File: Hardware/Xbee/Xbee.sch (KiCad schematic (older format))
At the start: 44 parts, among them J1 Alimentación, J2 Raspberry, J3 Pines 1, J4 Pines 2, J5 Programación, J6 Entrada, J7 Salida, K1 Rele12V, Q1 BC338, Q2 BC338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

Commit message: Started routing
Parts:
- D5, D6: footprint LED_THT:LED_D5.0mm -> Connector_PinSocket_2.54mm:PinSocket_1x02_P2.54mm_Vertical
- renumbered R4 to R1, R1 to R2, R2 to R3, R3 to R4
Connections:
- net GNDREF: now also J6.1 (Pin_1); no longer J6.2 (Pin_2)
- net Rasp.In: now also J6.2 (Pin_2); no longer J6.1 (Pin_1)

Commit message: Routing
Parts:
- C2: value 10u -> 1u
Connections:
- net Rasp.In renamed DIO2-Entrada
- net Rasp.Out renamed DIO2-Salida
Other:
- moved on the sheet: D4, D7, J6, J7, JP3, JP4, K1, Q2, Q3, R10, R13, R5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

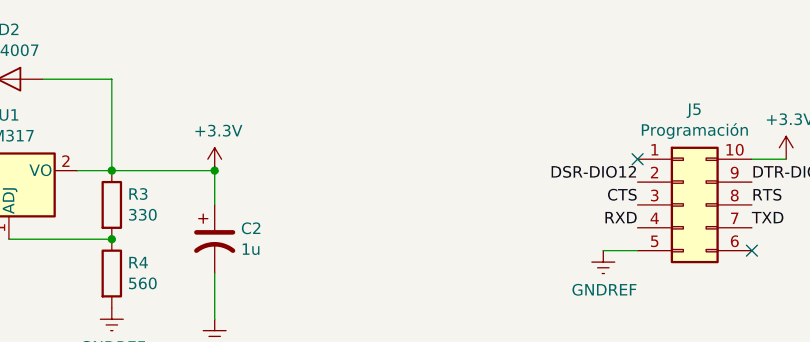
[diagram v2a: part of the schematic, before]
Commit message: SMD footprint
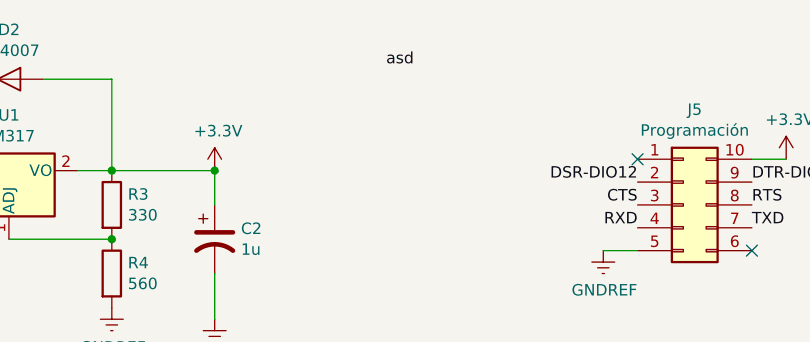
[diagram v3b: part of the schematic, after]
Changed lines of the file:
@@
 Text Label 8550 5350 0    50   ~ 0
 DIO2-Salida
+Text Label 4450 850  0    50   ~ 0
+asd
 $EndSCHEMATC

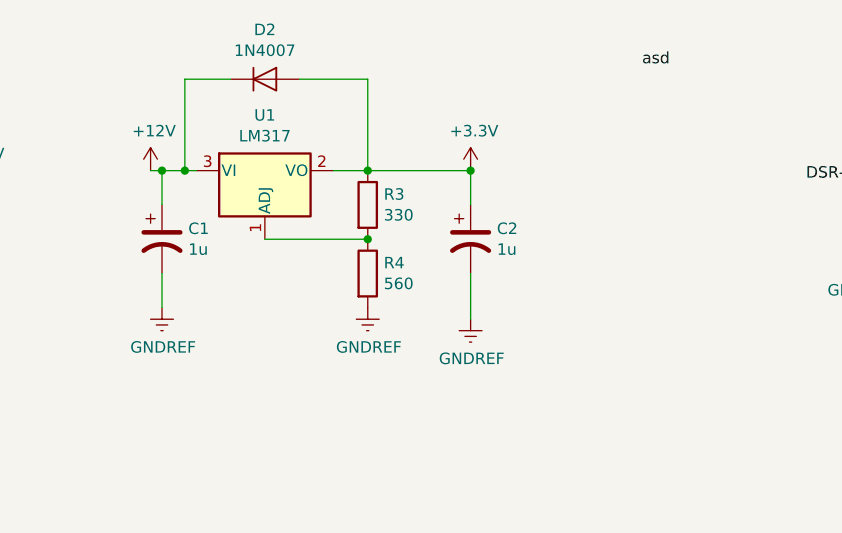
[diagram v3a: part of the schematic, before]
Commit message: SMD components
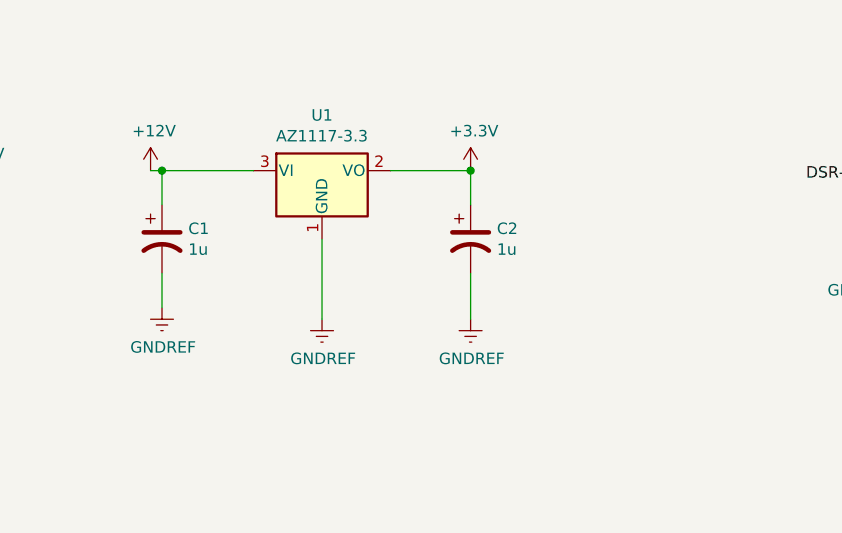
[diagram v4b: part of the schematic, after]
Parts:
- removed D2: 1N4007, Diode_THT:D_DO-41_SOD81_P10.16mm_Horizontal, symbol Xbee-rescue:1N4007-Diode
- removed R3: 330, Resistor_THT:R_Axial_DIN0207_L6.3mm_D2.5mm_P10.16mm_Horizontal, symbol Xbee-rescue:R-Device
- removed R4: 560, Resistor_THT:R_Axial_DIN0207_L6.3mm_D2.5mm_P10.16mm_Horizontal, symbol Xbee-rescue:R-Device
- removed U1: LM317, Package_TO_SOT_THT:TO-220-3_Vertical, symbol Xbee-rescue:LM317_3PinPackage-Regulator_Linear
- added U1: AZ1117-3.3, Package_TO_SOT_SMD:SOT-223-3_TabPin2, symbol Regulator_Linear:AZ1117-3.3
- D1, D7: footprint LED_THT:LED_D5.0mm -> LED_SMD:LED_0805_2012Metric
- U3: footprint Package_DIP:DIP-8_W7.62mm_Socket_LongPads -> Package_SO:SO-8_3.9x4.9mm_P1.27mm
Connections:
- net +12V: now also U1.3 (VI)
- net +3V3: now also U1.2 (VO)
- net GNDREF: now also U1.1 (GND)
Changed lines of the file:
@@
 	1550 1400 1400 1400
-$Comp
-L Xbee-rescue:LM317_3PinPackage-Regulator_Linear U1
-U 1 1 5C054755
-P 2800 1300
-F 0 "U1" H 2800 1542 50  0000 C CNN
-F 1 "LM317" H 2800 1451 50  0000 C CNN
-F 2 "Package_TO_SOT_THT:TO-220-3_Vertical" H 2800 1550 50  0001 C CIN
-F 3 "http://www.ti.com/lit/ds/symlink/lm317.pdf" H 2800 1300 50  0001 C CNN
-	1    2800 1300
-	1    0    0    -1
-$EndComp
-$Comp
-L Xbee-rescue:R-Device R3
-U 1 1 5C054800
-P 3250 1450
-F 0 "R3" H 3320 1496 50  0000 L CNN
-F 1 "330" H 3320 1405 50  0000 L CNN
-F 2 "Resistor_THT:R_Axial_DIN0207_L6.3mm_D2.5mm_P10.16mm_Horizontal" V 3180 1450 50  0001 C CNN
-F 3 "~" H 3250 1450 50  0001 C CNN
-	1    3250 1450
-	1    0    0    -1
-$EndComp
-$Comp
-L Xbee-rescue:R-Device R4
-U 1 1 5C054888
-P 3250 1750
-F 0 "R4" H 3320 1796 50  0000 L CNN
-F 1 "560" H 3320 1705 50  0000 L CNN
-F 2 "Resistor_THT:R_Axial_DIN0207_L6.3mm_D2.5mm_P10.16mm_Horizontal" V 3180 1750 50  0001 C CNN
-F 3 "~" H 3250 1750 50  0001 C CNN
-	1    3250 1750
-	1    0    0    -1
-$EndComp
 $Comp
 L Xbee-rescue:GNDREF-power #PWR012
 U 1 1 5C0548D0
-P 3250 1900
-F 0 "#PWR012" H 3250 1650 50  0001 C CNN
-F 1 "GNDREF" H 3255 1727 50  0000 C CNN
-F 2 "" H 3250 1900 50  0001 C CNN
-F 3 "" H 3250 1900 50  0001 C CNN
-	1    3250 1900
-	1    0    0    -1
-$EndComp
-Wire Wire Line
-	3250 1600 2800 1600
-Connection ~ 3250 1600
-Wire Wire Line
-	3100 1300 3250 1300
+P 3050 1950
+F 0 "#PWR012" H 3050 1700 50  0001 C CNN
+F 1 "GNDREF" H 3055 1777 50  0000 C CNN
+F 2 "" H 3050 1950 50  0001 C CNN
+F 3 "" H 3050 1950 50  0001 C CNN
+	1    3050 1950
+	1    0    0    -1
+$EndComp
 $Comp
 L Xbee-rescue:+12V-power #PWR07
@@
 Connection ~ 2350 1300
 Wire Wire Line
-	2350 1300 2450 1300
-Wire Wire Line
 	3700 1450 3700 1300
-Wire Wire Line
-	3700 1300 3250 1300
-Connection ~ 3250 1300
-$Comp
-L Xbee-rescue:1N4007-Diode D2
-U 1 1 5C054DA4
-P 2800 900
-F 0 "D2" H 2800 1116 50  0000 C CNN
-F 1 "1N4007" H 2800 1025 50  0000 C CNN
-F 2 "Diode_THT:D_DO-41_SOD81_P10.16mm_Horizontal" H 2800 725 50  0001 C CNN
-F 3 "http://www.vishay.com/docs/88503/1n4001.pdf" H 2800 900 50  0001 C CNN
-	1    2800 900
-	1    0    0    -1
-$EndComp
-Wire Wire Line
-	2650 900  2450 900
-Wire Wire Line
-	2450 900  2450 1300
-Connection ~ 2450 1300
-Wire Wire Line
-	2450 1300 2500 1300
-Wire Wire Line
-	2950 900  3250 900
-Wire Wire Line
-	3250 900  3250 1300
 $Comp
 L Xbee-rescue:SW_Push_Dual-Switch SW1
@@
 	1    0    0    -1
 $EndComp
-Connection ~ 3700 1300
 NoConn ~ 6750 3300
 Text Label 4550 3100 2    50   ~ 0
@@
 F 0 "D1" V 1738 6032 50  0000 R CNN
 F 1 "Assoc-RSSI" V 1647 6032 50  0000 R CNN
-F 2 "LED_THT:LED_D5.0mm" H 1700 6150 50  0001 C CNN
+F 2 "LED_SMD:LED_0805_2012Metric" H 1700 6150 50  0001 C CNN
 F 3 "~" H 1700 6150 50  0001 C CNN
 	1    1700 6150
@@
 F 0 "U3" H 9250 1567 50  0000 C CNN
 F 1 "LM358" H 9250 1476 50  0000 C CNN
-F 2 "Package_DIP:DIP-8_W7.62mm_Socket_LongPads" H 9250 1200 50  0001 C CNN
+F 2 "Package_SO:SO-8_3.9x4.9mm_P1.27mm" H 9250 1200 50  0001 C CNN
 F 3 "http://www.ti.com/lit/ds/symlink/lm2904-n.pdf" H 9250 1200 50  0001 C CNN
 	1    9250 1200
@@
 F 0 "U3" H 9250 2367 50  0000 C CNN
 F 1 "LM358" H 9250 2276 50  0000 C CNN
-F 2 "Package_DIP:DIP-8_W7.62mm_Socket_LongPads" H 9250 2000 50  0001 C CNN
+F 2 "Package_SO:SO-8_3.9x4.9mm_P1.27mm" H 9250 2000 50  0001 C CNN
 F 3 "http://www.ti.com/lit/ds/symlink/lm2904-n.pdf" H 9250 2000 50  0001 C CNN
 	2    9250 2000
@@
 F 0 "U3" H 7608 1396 50  0000 L CNN
 F 1 "LM358" H 7608 1305 50  0000 L CNN
-F 2 "Package_DIP:DIP-8_W7.62mm_Socket_LongPads" H 7650 1350 50  0001 C CNN
+F 2 "Package_SO:SO-8_3.9x4.9mm_P1.27mm" H 7650 1350 50  0001 C CNN
 F 3 "http://www.ti.com/lit/ds/symlink/lm2904-n.pdf" H 7650 1350 50  0001 C CNN
 	3    7650 1350
@@
 F 0 "D7" V 10638 5982 50  0000 R CNN
 F 1 "LED Salida" V 10547 5982 50  0000 R CNN
-F 2 "LED_THT:LED_D5.0mm" H 10600 6100 50  0001 C CNN
+F 2 "LED_SMD:LED_0805_2012Metric" H 10600 6100 50  0001 C CNN
 F 3 "~" H 10600 6100 50  0001 C CNN
 	1    10600 6100
@@
 Text Label 8550 5350 0    50   ~ 0
 DIO2-Salida
-Text Label 4450 850  0    50   ~ 0
-asd
+$Comp
+L Regulator_Linear:AZ1117-3.3 U1
+U 1 1 5D4F039F
+P 3050 1300
+F 0 "U1" H 3050 1542 50  0000 C CNN
+F 1 "AZ1117-3.3" H 3050 1451 50  0000 C CNN
+F 2 "Package_TO_SOT_SMD:SOT-223-3_TabPin2" H 3050 1550 50  0001 C CIN
+F 3 "https://www.diodes.com/assets/Datasheets/AZ1117.pdf" H 3050 1300 50  0001 C CNN
+	1    3050 1300
+	1    0    0    -1
+$EndComp
+Wire Wire Line
+	2350 1300 2750 1300
+Wire Wire Line
+	3350 1300 3700 1300
+Connection ~ 3700 1300
+Wire Wire Line
+	3050 1600 3050 1950
 $EndSCHEMATC

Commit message: Change names
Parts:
- D1: value Assoc-RSSI -> Blue Assoc-RSSI
- D7: value LED Salida -> LED Green Salida
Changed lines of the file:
@@
 P 1700 6150
 F 0 "D1" V 1738 6032 50  0000 R CNN
-F 1 "Assoc-RSSI" V 1647 6032 50  0000 R CNN
+F 1 "Blue Assoc-RSSI" V 1647 6032 50  0000 R CNN
 F 2 "LED_SMD:LED_0805_2012Metric" H 1700 6150 50  0001 C CNN
 F 3 "~" H 1700 6150 50  0001 C CNN
@@
 P 10600 6100
 F 0 "D7" V 10638 5982 50  0000 R CNN
-F 1 "LED Salida" V 10547 5982 50  0000 R CNN
+F 1 "LED Green Salida" V 10547 5982 50  0000 R CNN
 F 2 "LED_SMD:LED_0805_2012Metric" H 10600 6100 50  0001 C CNN
 F 3 "~" H 10600 6100 50  0001 C CNN

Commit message: SMD footprints, change LED's
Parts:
- removed Q1: BC338, Package_TO_SOT_THT:TO-92_Inline, symbol Xbee-rescue:BC338-Transistor_BJT
- removed R2: 68, Resistor_THT:R_Axial_DIN0207_L6.3mm_D2.5mm_P10.16mm_Horizontal, symbol Xbee-rescue:R-Device
- C1, C2: footprint Capacitor_THT:CP_Radial_D5.0mm_P2.50mm -> Capacitor_SMD:C_0805_2012Metric
- D3: footprint Diode_THT:D_DO-35_SOD27_P10.16mm_Horizontal -> Diode_SMD:D_SOT-23_ANK
- J5: footprint Connector_PinHeader_2.54mm:PinHeader_2x05_P2.54mm_Vertical -> Connector_PinHeader_2.54mm:PinHeader_2x05_P2.54mm_Horizontal
- R1: value 330 -> 360
- R13: value 680 -> 4k7
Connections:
- net at D1.2 (A): now also R1.1
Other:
- moved on the sheet: D1
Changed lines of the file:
@@
 F 0 "C1" H 2465 1646 50  0000 L CNN
 F 1 "1u" H 2465 1555 50  0000 L CNN
-F 2 "Capacitor_THT:CP_Radial_D5.0mm_P2.50mm" H 2350 1600 50  0001 C CNN
+F 2 "Capacitor_SMD:C_0805_2012Metric" H 2350 1600 50  0001 C CNN
 F 3 "~" H 2350 1600 50  0001 C CNN
 	1    2350 1600
@@
 F 0 "C2" H 3815 1646 50  0000 L CNN
 F 1 "1u" H 3815 1555 50  0000 L CNN
-F 2 "Capacitor_THT:CP_Radial_D5.0mm_P2.50mm" H 3700 1600 50  0001 C CNN
+F 2 "Capacitor_SMD:C_0805_2012Metric" H 3700 1600 50  0001 C CNN
 F 3 "~" H 3700 1600 50  0001 C CNN
 	1    3700 1600
@@
 Assoc.
 $Comp
-L Xbee-rescue:R-Device R2
-U 1 1 5C1A5BA0
-P 1700 5850
-F 0 "R2" H 1770 5896 50  0000 L CNN
-F 1 "68" H 1770 5805 50  0000 L CNN
-F 2 "Resistor_THT:R_Axial_DIN0207_L6.3mm_D2.5mm_P10.16mm_Horizontal" V 1630 5850 50  0001 C CNN
-F 3 "~" H 1700 5850 50  0001 C CNN
-	1    1700 5850
-	1    0    0    -1
-$EndComp
-$Comp
 L Xbee-rescue:LED_ALT-Device D1
 U 1 1 5C1A5C83
-P 1700 6150
-F 0 "D1" V 1738 6032 50  0000 R CNN
-F 1 "Blue Assoc-RSSI" V 1647 6032 50  0000 R CNN
-F 2 "LED_SMD:LED_0805_2012Metric" H 1700 6150 50  0001 C CNN
-F 3 "~" H 1700 6150 50  0001 C CNN
-	1    1700 6150
+P 1400 5650
+F 0 "D1" V 1438 5532 50  0000 R CNN
+F 1 "Blue Assoc-RSSI" V 1347 5532 50  0000 R CNN
+F 2 "LED_SMD:LED_0805_2012Metric" H 1400 5650 50  0001 C CNN
+F 3 "~" H 1400 5650 50  0001 C CNN
+	1    1400 5650
 	0    -1   -1   0
 $EndComp
@@
 L Xbee-rescue:GNDREF-power #PWR06
 U 1 1 5C1A5D78
-P 1700 6400
-F 0 "#PWR06" H 1700 6150 50  0001 C CNN
-F 1 "GNDREF" H 1705 6227 50  0000 C CNN
-F 2 "" H 1700 6400 50  0001 C CNN
-F 3 "" H 1700 6400 50  0001 C CNN
-	1    1700 6400
+P 1400 5900
+F 0 "#PWR06" H 1400 5650 50  0001 C CNN
+F 1 "GNDREF" H 1405 5727 50  0000 C CNN
+F 2 "" H 1400 5900 50  0001 C CNN
+F 3 "" H 1400 5900 50  0001 C CNN
+	1    1400 5900
 	1    0    0    -1
 $EndComp
@@
 F 0 "J5" H 5800 1867 50  0000 C CNN
 F 1 "Programación" H 5800 1776 50  0000 C CNN
-F 2 "Connector_PinHeader_2.54mm:PinHeader_2x05_P2.54mm_Vertical" H 5750 1450 50  0001 C CNN
+F 2 "Connector_PinHeader_2.54mm:PinHeader_2x05_P2.54mm_Horizontal" H 5750 1450 50  0001 C CNN
 F 3 "~" H 5750 1450 50  0001 C CNN
 	1    5750 1450
@@
 	0    -1   -1   0
 $EndComp
-$Comp
-L Xbee-rescue:BC338-Transistor_BJT Q1
-U 1 1 5C1A9F9C
-P 1600 5500
-F 0 "Q1" H 1791 5546 50  0000 L CNN
-F 1 "BC338" H 1791 5455 50  0000 L CNN
-F 2 "Package_TO_SOT_THT:TO-92_Inline" H 1800 5425 50  0001 L CIN
-F 3 "http://diotec.com/tl_files/diotec/files/pdf/datasheets/bc337" H 1600 5500 50  0001 L CNN
-	1    1600 5500
-	1    0    0    -1
-$EndComp
 Text Label 950  5250 2    50   ~ 0
 RSSI
@@
 P 1250 5500
 F 0 "R1" V 1043 5500 50  0000 C CNN
-F 1 "330" V 1134 5500 50  0000 C CNN
+F 1 "360" V 1134 5500 50  0000 C CNN
 F 2 "Resistor_THT:R_Axial_DIN0207_L6.3mm_D2.5mm_P10.16mm_Horizontal" V 1180 5500 50  0001 C CNN
 F 3 "~" H 1250 5500 50  0001 C CNN
@@
 	0    1    1    0
 $EndComp
-$Comp
-L Xbee-rescue:+3.3V-power #PWR05
-U 1 1 5C1AB37D
-P 1700 5300
-F 0 "#PWR05" H 1700 5150 50  0001 C CNN
-F 1 "+3.3V" H 1715 5473 50  0000 C CNN
-F 2 "" H 1700 5300 50  0001 C CNN
-F 3 "" H 1700 5300 50  0001 C CNN
-	1    1700 5300
-	1    0    0    -1
-$EndComp
-Wire Wire Line
-	1700 6300 1700 6400
+Wire Wire Line
+	1400 5800 1400 5900
 $Comp
 L Xbee-rescue:Screw_Terminal_01x02-Connector J7
@@
 F 0 "D3" V 8200 1600 50  0000 L CNN
 F 1 "Zener 5V" V 8300 1450 50  0000 L CNN
-F 2 "Diode_THT:D_DO-35_SOD27_P10.16mm_Horizontal" H 8150 1800 50  0001 C CNN
+F 2 "Diode_SMD:D_SOT-23_ANK" H 8150 1800 50  0001 C CNN
 F 3 "~" H 8150 1800 50  0001 C CNN
 	1    8150 1800
@@
 P 10600 5650
 F 0 "R13" H 10670 5696 50  0000 L CNN
-F 1 "680" H 10670 5605 50  0000 L CNN
+F 1 "4k7" H 10670 5605 50  0000 L CNN
 F 2 "Resistor_THT:R_Axial_DIN0207_L6.3mm_D2.5mm_P10.16mm_Horizontal" V 10530 5650 50  0001 C CNN
 F 3 "~" H 10600 5650 50  0001 C CNN
